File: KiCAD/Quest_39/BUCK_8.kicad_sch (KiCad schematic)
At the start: 32 parts, among them U36 AD626ANZ, U37 INA226, U38 LTM4611EV-PBF, U39 MCP4151-502E/SN

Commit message: Fixed INA226 schem. mistake and further layout work
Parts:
- added C138: 100nF, Capacitor_SMD:C_0603_1608Metric, symbol Device:C
- renumbered C126 to C134, C127 to C135, C128 to C136, C129 to C137, C130 to C139, C131 to C140, C132 to C141, C133 to C142, C134 to C143, C135 to C144, C136 to C145, C137 to C146, C138 to C147, C139 to C148
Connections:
- net +5V: now also C138.1
- net GND: now also C138.2
- net PV_POS: no longer C134.1, C135.1, C136.1, C137.1, R73.2, R75.1, R78.1, U38.A1 (VIN), U38.A2 (VIN), U38.A3 (VIN), U38.A4 (VIN), U38.A5 (VIN), U38.A6 (VIN), U38.B1 (VIN), U38.B2 (VIN), U38.B3 (VIN), U38.B4 (VIN), U38.B5 (VIN), U38.B6 (VIN), U38.C1 (VIN), U38.C2 (VIN), U38.C3 (VIN), U38.C4 (VIN), U38.C5 (VIN), U38.C6 (VIN)
- net Vin-: no longer TP63.1, U36.5 (OUT), U37.8 (Vbus)
- new net: TP63.1, U36.5 (OUT), U37.8 (Vbus)
- new net BUCK_VIN: C134.1, C135.1, C136.1, C137.1, R73.2, R75.1, R78.1, U38.A1 (VIN), U38.A2 (VIN), U38.A3 (VIN), U38.A4 (VIN), U38.A5 (VIN), U38.A6 (VIN), U38.B1 (VIN), U38.B2 (VIN), U38.B3 (VIN), U38.B4 (VIN), U38.B5 (VIN), U38.B6 (VIN), U38.C1 (VIN), U38.C2 (VIN), U38.C3 (VIN), U38.C4 (VIN), U38.C5 (VIN), U38.C6 (VIN)

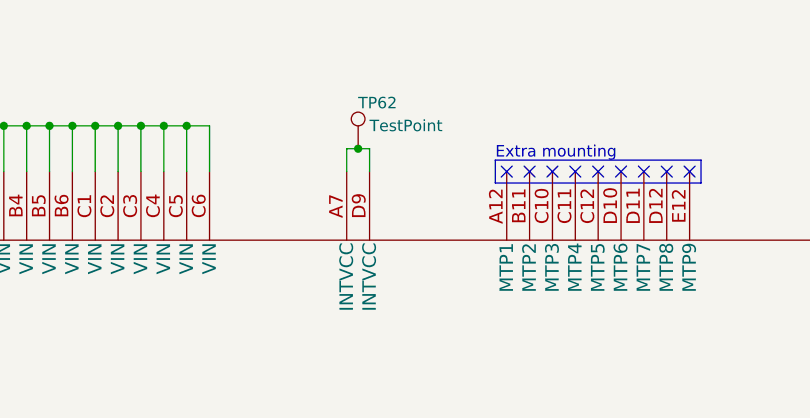
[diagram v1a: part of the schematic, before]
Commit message: Partial wiring of first buck converter section PCB layout
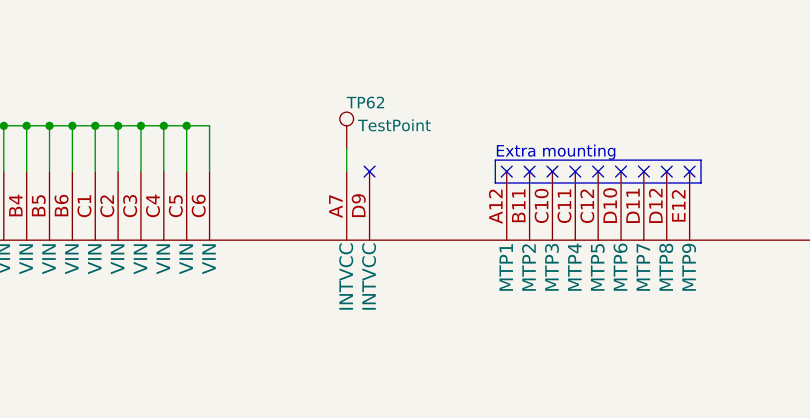
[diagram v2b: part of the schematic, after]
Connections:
- net at TP62.1, U38.A7 (INTVCC): no longer U38.D9 (INTVCC)
- no-connect marks 12 -> 13
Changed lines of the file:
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@@
   (junction (at 177.8 36.83) (diameter 0) (color 0 0 0 0)
-  )
-  (junction (at 234.95 39.37) (diameter 0) (color 0 0 0 0)
   )
   (junction (at 383.54 158.75) (diameter 0) (color 0 0 0 0)
@@
   (no_connect (at 261.62 41.91))
   (no_connect (at 264.16 41.91))
+  (no_connect (at 236.22 41.91))
   (no_connect (at 266.7 41.91))
   (no_connect (at 60.96 68.58))
@@
     (stroke (width 0) (type default) (color 0 0 0 0))
   )
+  (wire (pts (xy 233.68 41.91) (xy 233.68 39.37))
+    (stroke (width 0) (type default) (color 0 0 0 0))
+  )
   (wire (pts (xy 223.52 201.93) (xy 226.06 201.93))
     (stroke (width 0) (type default) (color 0 0 0 0))
@@
     (stroke (width 0) (type default) (color 0 0 0 0))
   )
-  (wire (pts (xy 236.22 39.37) (xy 236.22 41.91))
-    (stroke (width 0) (type default) (color 0 0 0 0))
-  )
   (wire (pts (xy 322.58 176.53) (xy 353.06 176.53))
     (stroke (width 0) (type default) (color 0 0 0 0))
@@
     (stroke (width 0) (type default) (color 0 0 0 0))
   )
-  (wire (pts (xy 234.95 39.37) (xy 236.22 39.37))
-    (stroke (width 0) (type default) (color 0 0 0 0))
-  )
   (wire (pts (xy 130.81 36.83) (xy 130.81 38.1))
     (stroke (width 0) (type default) (color 0 0 0 0))
@@
     (stroke (width 0) (type default) (color 0 0 0 0))
   )
-  (wire (pts (xy 233.68 39.37) (xy 234.95 39.37))
-    (stroke (width 0) (type default) (color 0 0 0 0))
-  )
   (wire (pts (xy 236.22 201.93) (xy 238.76 201.93))
     (stroke (width 0) (type default) (color 0 0 0 0))
@@
   )
   (wire (pts (xy 129.54 113.03) (xy 137.16 113.03))
-    (stroke (width 0) (type default) (color 0 0 0 0))
-  )
-  (wire (pts (xy 233.68 41.91) (xy 233.68 39.37))
     (stroke (width 0) (type default) (color 0 0 0 0))
   )
@@
     (pin "7")
     (pin "8")
-  )
-  (symbol (lib_id "Connector:TestPoint") (at 234.95 39.37 0) (unit 1)
-    (in_bom yes) (on_board yes)
-    (property "Reference" "TP62" (id 0) (at 234.95 34.29 0)
-      (effects (font (size 1.27 1.27)) (justify left))
-    )
-    (property "Value" "TestPoint" (id 1) (at 236.22 36.83 0)
-      (effects (font (size 1.27 1.27)) (justify left))
-    )
-    (property "Footprint" "TestPoint:TestPoint_Pad_D2.0mm" (id 2) (at 240.03 39.37 0)
-      (effects (font (size 1.27 1.27)) hide)
-    )
-    (property "Datasheet" "~" (id 3) (at 240.03 39.37 0)
-      (effects (font (size 1.27 1.27)) hide)
-    )
-    (pin "1")
   )
   (symbol (lib_id "Connector:TestPoint") (at 129.54 113.03 90) (unit 1)
@@
       (effects (font (size 1.27 1.27)) hide)
     )
+    (pin "1")
+  )
+  (symbol (lib_id "Connector:TestPoint") (at 233.68 39.37 0) (unit 1)
+    (in_bom yes) (on_board yes)
+    (property "Reference" "TP62" (id 0) (at 233.68 34.29 0)
+      (effects (font (size 1.27 1.27)) (justify left))
+    )
+    (property "Value" "TestPoint" (id 1) (at 234.95 36.83 0)
+      (effects (font (size 1.27 1.27)) (justify left))
+    )
+    (property "Footprint" "TestPoint:TestPoint_Pad_D2.0mm" (id 2) (at 238.76 39.37 0)
+      (effects (font (size 1.27 1.27)) hide)
+    )
+    (property "Datasheet" "~" (id 3) (at 238.76 39.37 0)
+      (effects (font (size 1.27 1.27)) hide)
+    )

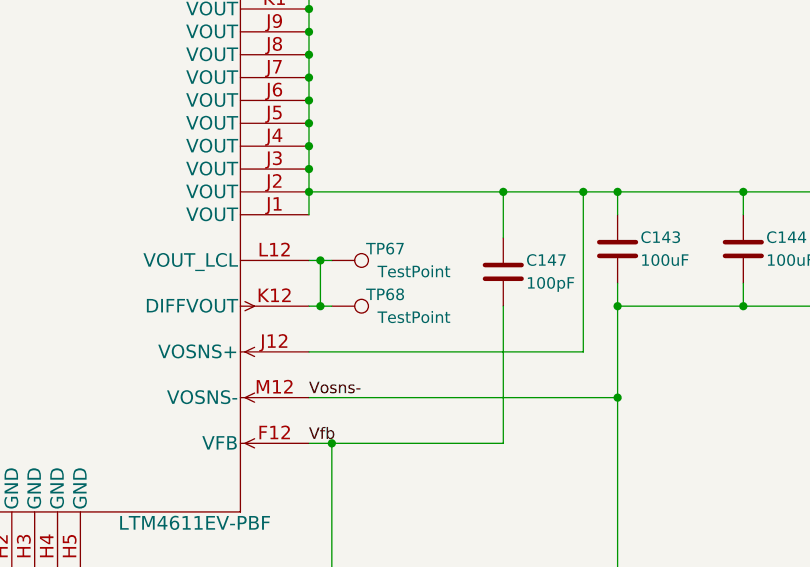
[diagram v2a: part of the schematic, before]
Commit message: Added 3rd buck converter section
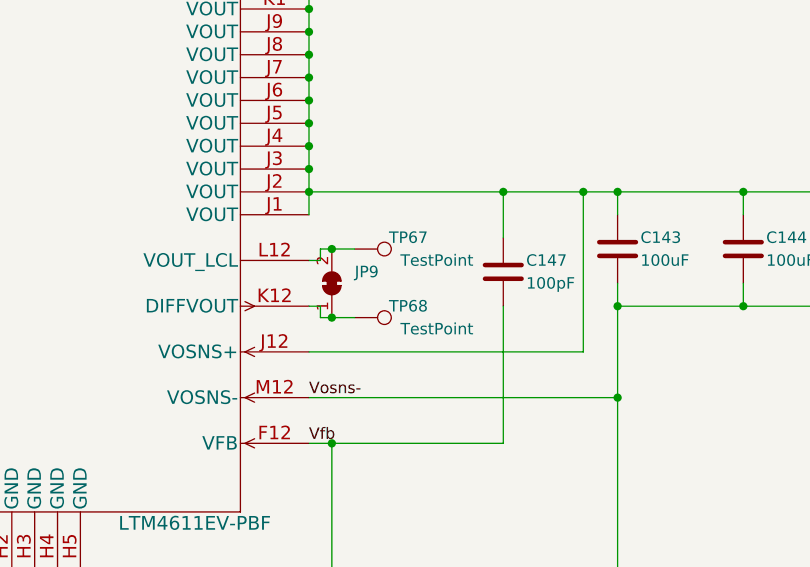
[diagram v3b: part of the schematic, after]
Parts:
- added JP9: SolderJumper_2_Bridged, Jumper:SolderJumper-2_P1.3mm_Bridged_RoundedPad1.0x1.5mm, symbol Jumper:SolderJumper_2_Bridged
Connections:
- net at TP67.1, U38.L12 (VOUT_LCL): now also JP9.2 (B); no longer TP68.1, U38.K12 (DIFFVOUT)
- new net: JP9.1 (A), TP68.1, U38.K12 (DIFFVOUT)
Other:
- moved on the sheet: TP67, TP68

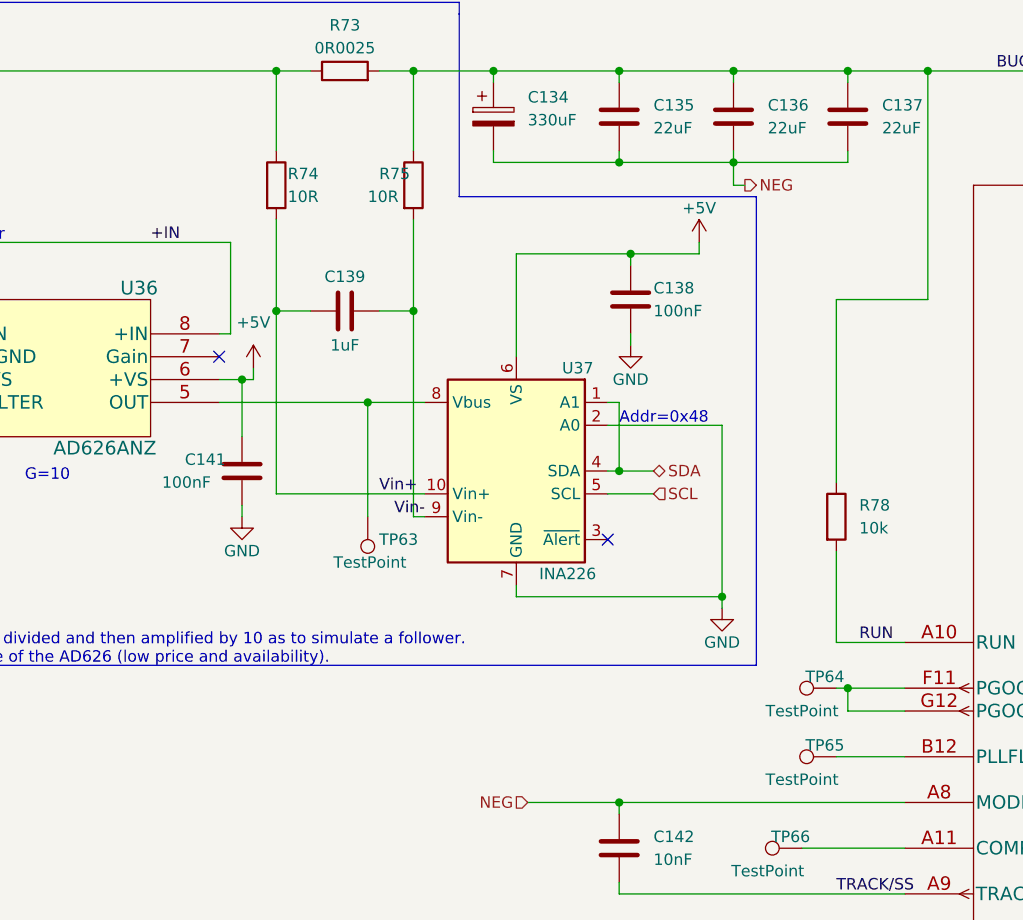
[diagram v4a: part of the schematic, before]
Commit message: Redid layout for the LTM4611EV Buck-converters (Issues with net-assignment to IC pads)
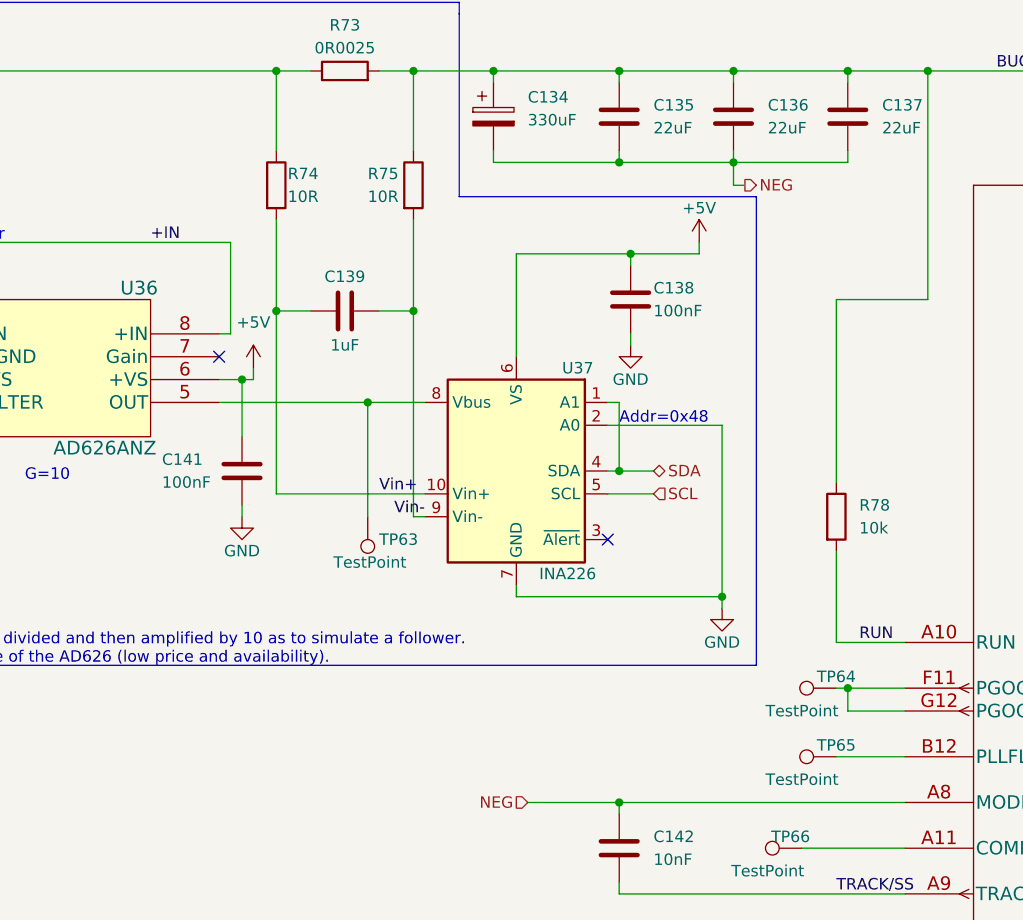
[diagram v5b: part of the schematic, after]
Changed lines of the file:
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@@
   (symbol (lib_id "Connector:TestPoint") (at 129.54 113.03 90) (unit 1)
     (in_bom yes) (on_board yes)
-    (property "Reference" "TP65" (id 0) (at 128.27 111.76 90))
+    (property "Reference" "TP65" (id 0) (at 129.54 111.76 90))
     (property "Value" "TestPoint" (id 1) (at 125.73 115.57 90))
     (property "Footprint" "TestPoint:TestPoint_Pad_D2.0mm" (id 2) (at 129.54 107.95 0)
@@
   (symbol (lib_id "Device:R") (at 82.55 49.53 0) (unit 1)
     (in_bom yes) (on_board yes)
-    (property "Reference" "R75" (id 0) (at 78.74 48.26 0)
+    (property "Reference" "R75" (id 0) (at 77.47 48.26 0)
       (effects (font (size 1.27 1.27)) (justify left))
     )
@@
   (symbol (lib_id "Device:C") (at 63.5 81.28 0) (unit 1)
     (in_bom yes) (on_board yes)
-    (property "Reference" "C141" (id 0) (at 57.15 80.01 0)
+    (property "Reference" "C141" (id 0) (at 54.61 80.01 0)
       (effects (font (size 1.27 1.27)) (justify left))
     )
@@
   (symbol (lib_id "Connector:TestPoint") (at 129.54 105.41 90) (unit 1)
     (in_bom yes) (on_board yes)
-    (property "Reference" "TP64" (id 0) (at 128.27 104.14 90))
+    (property "Reference" "TP64" (id 0) (at 129.54 104.14 90))
     (property "Value" "TestPoint" (id 1) (at 125.73 107.95 90))
     (property "Footprint" "TestPoint:TestPoint_Pad_D2.0mm" (id 2) (at 129.54 100.33 0)

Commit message: Added all the SolidWorks files, edited README
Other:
- title: (none) -> BUCK_8
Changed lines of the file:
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@@
 (kicad_sch (version 20211123) (generator eeschema)
   (paper "A3")
+  (title_block
+    (title "BUCK_8")
+    (date "2023-01-31")
+    (rev "1.0")
+  )
   (junction (at 167.64 201.93) (diameter 0) (color 0 0 0 0)
   )
